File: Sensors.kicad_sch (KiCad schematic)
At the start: 2 parts

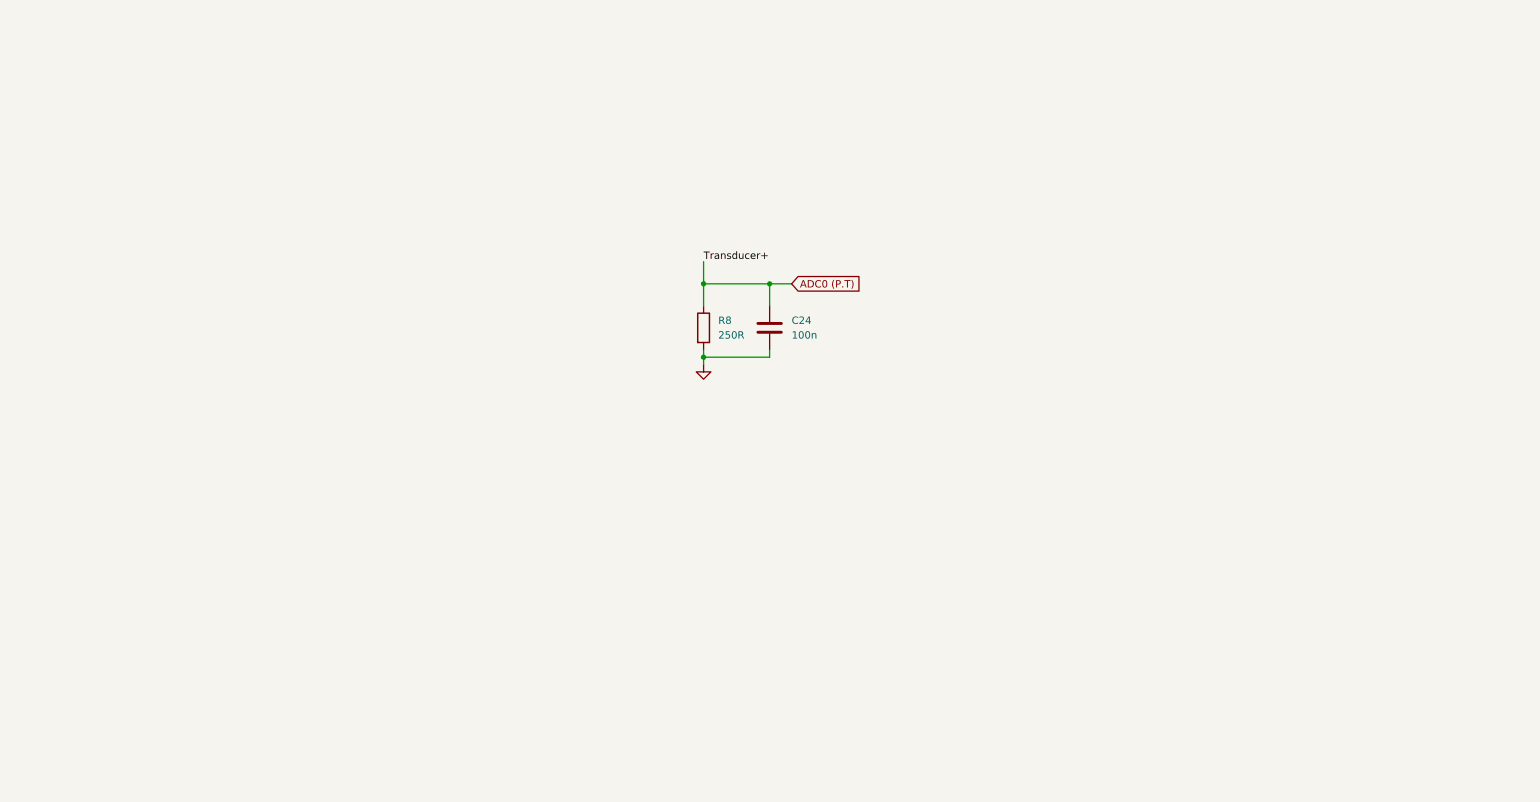
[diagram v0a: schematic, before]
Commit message: Changes before syncing to main. Adding crystal as well as Thermocouple sensor and buck 3.3V step down
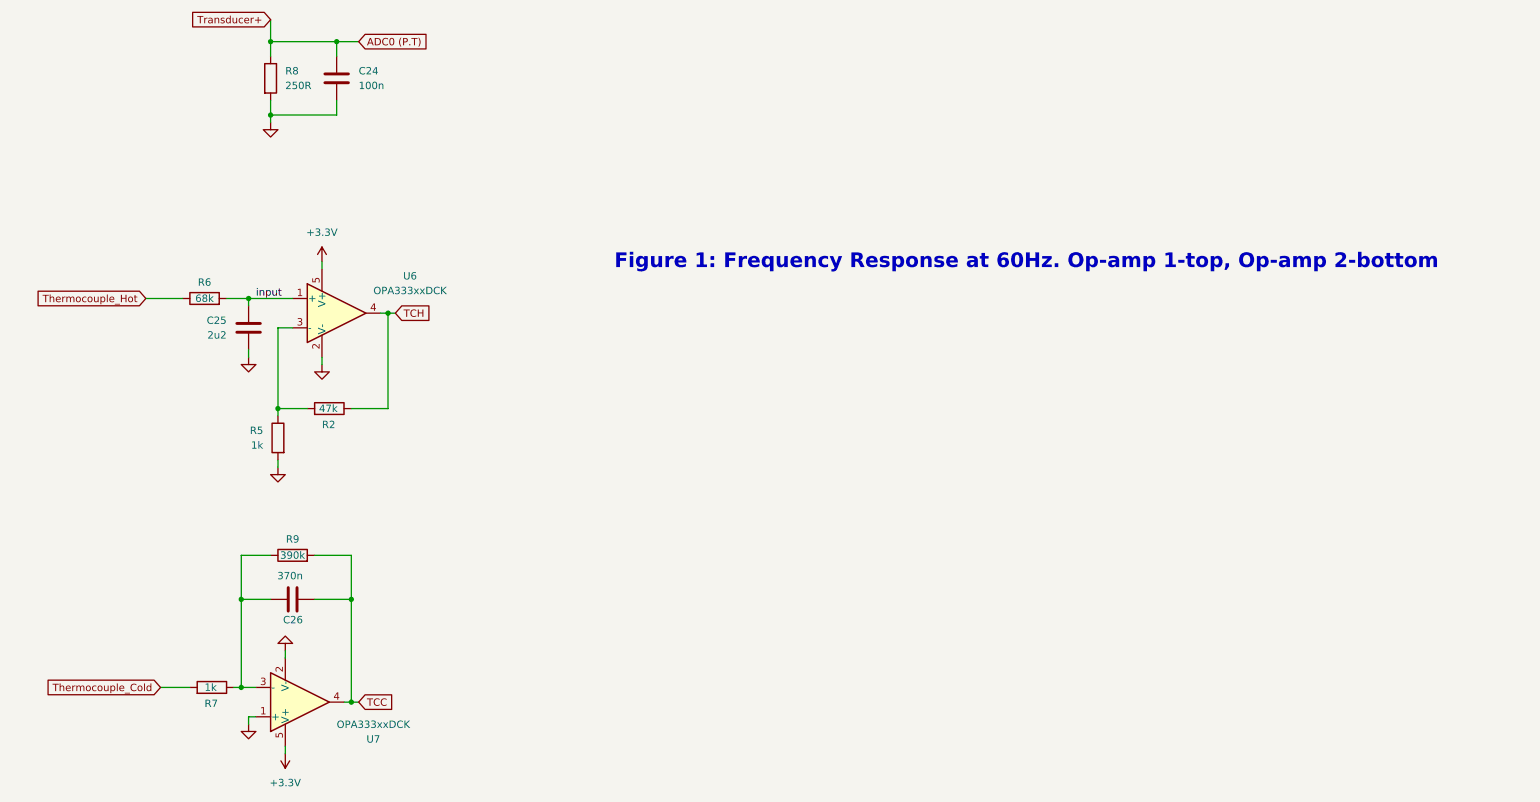
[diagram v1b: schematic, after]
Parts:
- added C25: 2u2, symbol Device:C
- added C26: 370n, symbol Device:C
- added R2: 47k, symbol Device:R
- added R5, R7: 1k, symbol Device:R
- added R6: 68k, symbol Device:R
- added R9: 390k, symbol Device:R
- added U6, U7: OPA333xxDCK, Package_TO_SOT_SMD:SOT-353_SC-70-5, symbol Amplifier_Operational:OPA333xxDCK
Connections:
- net GND: now also C25.2, R5.2, U6.2 (V-), U7.1 (+), U7.2 (V-)
- new net: R2.2, R5.1, U6.3 (-)
- new net: C26.1, R7.1, R9.1, U7.3 (-)
- new net +3.3V: U6.5 (V+), U7.5 (V+)
- new net TCC: C26.2, R9.2, U7.4
- new net TCH: R2.1, U6.4
- new net Thermocouple_Cold: R7.2
- new net Thermocouple_Hot: R6.1
- new net input: C25.1, R6.2, U6.1 (+)
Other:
- note added: "Figure 1: Frequency Response at 60Hz. Op-amp 1-top, Op-amp 2-bottom"
- moved on the sheet: C24, R8

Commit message: Added changes to pass ERC check
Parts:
- renumbered C25 to C10, C26 to C11, C24 to C12, R5 to R10, R9 to R11, R2 to R12, R6 to R7, R7 to R8, R8 to R9, U7 to U3, U6 to U4
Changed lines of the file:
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@@
 		(dnp no)
 		(fields_autoplaced yes)
-		(property "Reference" "#PWR051"
+		(property "Reference" "#PWR017"
 			(at 71.12 138.43 0)
 			(hide yes)
@@
 			(project "LRE_Controller"
 				(path "/b27bef7b-72d9-475e-9417-80b6d20be6a1/d792bc85-680a-4688-bc00-a30b1ff2ba64"
-					(reference "#PWR051")
+					(reference "#PWR017")
 					(unit 1)
 				)
@@
 		(dnp no)
 		(fields_autoplaced yes)
-		(property "Reference" "U6"
+		(property "Reference" "U4"
 			(at 93.98 98.9898 0)
 			(show_name no)
@@
 			(project "LRE_Controller"
 				(path "/b27bef7b-72d9-475e-9417-80b6d20be6a1/d792bc85-680a-4688-bc00-a30b1ff2ba64"
-					(reference "U6")
+					(reference "U4")
 					(unit 1)
 				)
@@
 		(in_pos_files yes)
 		(dnp no)
-		(property "Reference" "R6"
+		(property "Reference" "R7"
 			(at 58.42 100.076 90)
 			(show_name no)
@@
 			(project "LRE_Controller"
 				(path "/b27bef7b-72d9-475e-9417-80b6d20be6a1/d792bc85-680a-4688-bc00-a30b1ff2ba64"
-					(reference "R6")
+					(reference "R7")
 					(unit 1)
 				)
@@
 		(dnp no)
 		(fields_autoplaced yes)
-		(property "Reference" "C24"
+		(property "Reference" "C12"
 			(at 85.09 63.4999 0)
 			(show_name no)
@@
 			(project "LRE_Controller"
 				(path "/b27bef7b-72d9-475e-9417-80b6d20be6a1/d792bc85-680a-4688-bc00-a30b1ff2ba64"
-					(reference "C24")
+					(reference "C12")
 					(unit 1)
 				)
@@
 		(in_pos_files yes)
 		(dnp no)
-		(property "Reference" "C26"
+		(property "Reference" "C11"
 			(at 75.438 158.496 90)
 			(show_name no)
@@
 			(project "LRE_Controller"
 				(path "/b27bef7b-72d9-475e-9417-80b6d20be6a1/d792bc85-680a-4688-bc00-a30b1ff2ba64"
-					(reference "C26")
+					(reference "C11")
 					(unit 1)
 				)
@@
 		(in_pos_files yes)
 		(dnp no)
-		(property "Reference" "R7"
+		(property "Reference" "R8"
 			(at 58.42 172.974 90)
 			(show_name no)
@@
 			(project "LRE_Controller"
 				(path "/b27bef7b-72d9-475e-9417-80b6d20be6a1/d792bc85-680a-4688-bc00-a30b1ff2ba64"
-					(reference "R7")
+					(reference "R8")
 					(unit 1)
 				)
@@
 		(in_pos_files yes)
 		(dnp no)
-		(property "Reference" "U7"
+		(property "Reference" "U3"
 			(at 87.63 179.1402 0)
 			(show_name no)
@@
 			(project "LRE_Controller"
 				(path "/b27bef7b-72d9-475e-9417-80b6d20be6a1/d792bc85-680a-4688-bc00-a30b1ff2ba64"
-					(reference "U7")
+					(reference "U3")
 					(unit 1)
 				)
@@
 		(in_pos_files yes)
 		(dnp no)
-		(property "Reference" "R5"
+		(property "Reference" "R10"
 			(at 68.58 125.7299 0)
 			(show_name no)
@@
 			(project "LRE_Controller"
 				(path "/b27bef7b-72d9-475e-9417-80b6d20be6a1/d792bc85-680a-4688-bc00-a30b1ff2ba64"
-					(reference "R5")
+					(reference "R10")
 					(unit 1)
 				)
@@
 		(dnp no)
 		(fields_autoplaced yes)
-		(property "Reference" "#PWR050"
+		(property "Reference" "#PWR014"
 			(at 66.04 119.38 0)
 			(hide yes)
@@
 			(project "LRE_Controller"
 				(path "/b27bef7b-72d9-475e-9417-80b6d20be6a1/d792bc85-680a-4688-bc00-a30b1ff2ba64"
-					(reference "#PWR050")
+					(reference "#PWR014")
 					(unit 1)
 				)
@@
 		(dnp no)
 		(fields_autoplaced yes)
-		(property "Reference" "#PWR014"
+		(property "Reference" "#PWR020"
 			(at 78.74 100.33 0)
 			(hide yes)
@@
 			(project "LRE_Controller"
 				(path "/b27bef7b-72d9-475e-9417-80b6d20be6a1/d792bc85-680a-4688-bc00-a30b1ff2ba64"
-					(reference "#PWR014")
+					(reference "#PWR020")
 					(unit 1)
 				)
@@
 		(dnp no)
 		(fields_autoplaced yes)
-		(property "Reference" "#PWR053"
+		(property "Reference" "#PWR015"
 			(at 66.04 182.88 0)
 			(hide yes)
@@
 			(project "LRE_Controller"
 				(path "/b27bef7b-72d9-475e-9417-80b6d20be6a1/d792bc85-680a-4688-bc00-a30b1ff2ba64"
-					(reference "#PWR053")
+					(reference "#PWR015")
 					(unit 1)
 				)
@@
 		(dnp no)
 		(fields_autoplaced yes)
-		(property "Reference" "R8"
+		(property "Reference" "R9"
 			(at 72.39 63.4999 0)
 			(show_name no)
@@
 			(project "LRE_Controller"
 				(path "/b27bef7b-72d9-475e-9417-80b6d20be6a1/d792bc85-680a-4688-bc00-a30b1ff2ba64"
-					(reference "R8")
+					(reference "R9")
 					(unit 1)
 				)
@@
 		(in_pos_files yes)
 		(dnp no)
-		(property "Reference" "C25"
+		(property "Reference" "C10"
 			(at 62.23 106.6799 0)
 			(show_name no)
@@
 			(project "LRE_Controller"
 				(path "/b27bef7b-72d9-475e-9417-80b6d20be6a1/d792bc85-680a-4688-bc00-a30b1ff2ba64"
-					(reference "C25")
+					(reference "C10")
 					(unit 1)
 				)
@@
 		(in_pos_files yes)
 		(dnp no)
-		(property "Reference" "R9"
+		(property "Reference" "R11"
 			(at 73.66 144.526 90)
 			(show_name no)
@@
 			(project "LRE_Controller"
 				(path "/b27bef7b-72d9-475e-9417-80b6d20be6a1/d792bc85-680a-4688-bc00-a30b1ff2ba64"
-					(reference "R9")
+					(reference "R11")
 					(unit 1)
 				)
@@
 		(dnp no)
 		(fields_autoplaced yes)
-		(property "Reference" "#PWR052"
+		(property "Reference" "#PWR018"
 			(at 72.39 157.48 0)
 			(hide yes)
@@
 			(project "LRE_Controller"
 				(path "/b27bef7b-72d9-475e-9417-80b6d20be6a1/d792bc85-680a-4688-bc00-a30b1ff2ba64"
-					(reference "#PWR052")
+					(reference "#PWR018")
 					(unit 1)
 				)
@@
 		(dnp no)
 		(fields_autoplaced yes)
-		(property "Reference" "#PWR049"
+		(property "Reference" "#PWR021"
 			(at 78.74 120.65 0)
 			(hide yes)
@@
 			(project "LRE_Controller"
 				(path "/b27bef7b-72d9-475e-9417-80b6d20be6a1/d792bc85-680a-4688-bc00-a30b1ff2ba64"
-					(reference "#PWR049")
+					(reference "#PWR021")
 					(unit 1)
 				)
@@
 		(dnp no)
 		(fields_autoplaced yes)
-		(property "Reference" "#PWR015"
+		(property "Reference" "#PWR019"
 			(at 72.39 177.8 0)
 			(hide yes)
@@
 			(project "LRE_Controller"
 				(path "/b27bef7b-72d9-475e-9417-80b6d20be6a1/d792bc85-680a-4688-bc00-a30b1ff2ba64"
-					(reference "#PWR015")
+					(reference "#PWR019")
 					(unit 1)
 				)
@@
 		(in_pos_files yes)
 		(dnp no)
-		(property "Reference" "R2"
+		(property "Reference" "R12"
 			(at 78.74 124.714 90)
 			(show_name no)
@@
 			(project "LRE_Controller"
 				(path "/b27bef7b-72d9-475e-9417-80b6d20be6a1/d792bc85-680a-4688-bc00-a30b1ff2ba64"
-					(reference "R2")
+					(reference "R12")
 					(unit 1)
 				)
@@
 		(dnp no)
 		(fields_autoplaced yes)
-		(property "Reference" "#PWR027"
+		(property "Reference" "#PWR016"
 			(at 69.85 78.74 0)
 			(hide yes)
@@
 			(project "LRE_Controller"
 				(path "/b27bef7b-72d9-475e-9417-80b6d20be6a1/d792bc85-680a-4688-bc00-a30b1ff2ba64"
-					(reference "#PWR027")
-					(unit 1)
-				)
+					(reference "#PWR016")
+					(unit 1)
+				)

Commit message: added footprints to every component except inductors. That will be in the next commit
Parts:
- C10, C11, C12: footprint (none) -> Capacitor_SMD:C_0402_1005Metric
- R10, R11, R12, R7, R8, R9: footprint (none) -> Resistor_SMD:R_0402_1005Metric
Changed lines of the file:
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@@
 			)
 		)
-		(property "Footprint" ""
+		(property "Footprint" "Resistor_SMD:R_0402_1005Metric"
 			(at 58.42 104.648 90)
 			(hide yes)
@@
 			)
 		)
-		(property "Footprint" ""
+		(property "Footprint" "Capacitor_SMD:C_0402_1005Metric"
 			(at 82.2452 68.58 0)
 			(hide yes)
@@
 			)
 		)
-		(property "Footprint" ""
+		(property "Footprint" "Capacitor_SMD:C_0402_1005Metric"
 			(at 77.47 155.9052 0)
 			(hide yes)
@@
 			)
 		)
-		(property "Footprint" ""
+		(property "Footprint" "Resistor_SMD:R_0402_1005Metric"
 			(at 59.69 171.958 90)
 			(hide yes)
@@
 			)
 		)
-		(property "Footprint" ""
+		(property "Footprint" "Resistor_SMD:R_0402_1005Metric"
 			(at 72.898 127 90)
 			(hide yes)
@@
 			)
 		)
-		(property "Footprint" ""
+		(property "Footprint" "Resistor_SMD:R_0402_1005Metric"
 			(at 68.072 64.77 90)
 			(hide yes)
@@
 			)
 		)
-		(property "Footprint" ""
+		(property "Footprint" "Capacitor_SMD:C_0402_1005Metric"
 			(at 65.0748 111.76 0)
 			(hide yes)
@@
 			)
 		)
-		(property "Footprint" ""
+		(property "Footprint" "Resistor_SMD:R_0402_1005Metric"
 			(at 73.66 149.098 90)
 			(hide yes)
@@
 			)
 		)
-		(property "Footprint" ""
+		(property "Footprint" "Resistor_SMD:R_0402_1005Metric"
 			(at 80.01 123.698 90)
 			(hide yes)
